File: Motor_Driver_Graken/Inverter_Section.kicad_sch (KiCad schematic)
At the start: 93 parts, among them Q1 NMOS, Q2 NMOS, Q3 NMOS, Q4 NMOS, Q5 NMOS, Q6 NMOS, U10 UCC21520DW, U6 UCC21520DW, U9 UCC21520DW

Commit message: Schematic Changes
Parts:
- removed C100: C_Small, symbol Device:C_Small
- removed R44: R_Small, symbol Device:R_Small
- added C120: 4.7u, symbol Device:C_Small
- added D11: D, symbol Device:D
- added R115: 2.2R, symbol Device:R_Small
- added R116: 10K, symbol Device:R_Small
- C42, C48, C50, C64, C66, C71, C73, C75, C76, C77, C78, C80, C89, C91: value C_Small -> 4.7u
- C43, C44, C51, C56, C65, C67, C72, C74, C79, C81, C90, C92, C97, C98, C99: value C_Small -> 0.1u
- C49, C70, C96: value C_Small -> 100n
- C52, C53, C54, C55, C68, C69, C93, C94, C95: value C_Small -> 270p
- R18, R42: value R_Small -> 10K
- R20, R21, R22, R28, R29, R30, R35, R37, R38: value R_Small -> 60.4R
- R23, R24, R26, R31, R32, R33, R39, R40, R41: value R_Small -> 2.2K
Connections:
- net 15V_ISOa: now also R115.2; no longer U6.16 (VDDA)
- net 15V_ISOb: now also C71.1, C120.1; no longer C55.1, C73.1
- net 15V_ISOc: now also C75.1, C79.1, C99.1; no longer C76.1, C97.1, C98.1
- net DIS: now also C69.1, R38.1, R38.2, R41.2; no longer C70.1, R39.1, R39.2, R42.2
- net GND2: now also C71.2, C73.1, C76.1, C97.1, C98.1, C120.2; no longer C55.2, C75.1, C79.1, C99.1
- net GNDD: now also C55.2, R39.1, R42.2, R116.2; no longer C71.2, R35.2, R42.1
- net PWM_W_HIGH: now also R35.1; no longer R37.1
- net PWM_W_LOW: now also R37.1; no longer R38.1
- net at C96.1, U10.6 (DT): now also R42.1
- removed net INA: C52.1, C68.1, C93.1, R20.2, R23.2, R28.2, R31.2, R37.2, R40.2, U10.1 (INA), U6.1 (INA), U9.1 (INA)
- removed net INB: C53.1, C69.1, C94.1, R21.2, R24.2, R29.2, R32.2, R38.2, R41.2, U10.2 (INB), U6.2 (INB), U9.2 (INB)
- new net: C70.1, R116.1, U9.6 (DT)
- new net: D11.1 (K), U6.16 (VDDA)
- new net: D11.2 (A), R115.1
- new net INuH: C52.1, R20.2, R23.2, U6.1 (INA)
- new net INuL: C53.1, R21.2, R24.2, U6.2 (INB)
- new net INvH: C55.1, R28.2, R31.2, U9.1 (INA)
- new net INvL: C68.1, R29.2, R32.2, U9.2 (INB)
- new net INwH: C93.1, R35.2, R39.2, U10.1 (INA)
- new net INwL: C94.1, R37.2, R40.2, U10.2 (INB)
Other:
- moved on the sheet: C48, C49, C52, C91, C92, Q5, Q6, R18, R20, R21, R22, R23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

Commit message: Flim Capacitors
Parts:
- removed C61, C62, C63: C_Small, symbol Device:C_Small
- removed R39, R40, R41: 2.2K, symbol Device:R_Small
- removed R47, R48, R49: R_Small, symbol Device:R_Small
- added C100, C121: 470u, symbol Device:C_Polarized
- added C157, C158, C159: 470u, symbol Device:C_Small
- added R117, R118, R44: 2.2K, symbol Device:R_Small
- C34, C59, C60: value C_Polarized -> 470u
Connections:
- net 120Vdc: now also C100.1, C121.1, C157.1, C158.1, C159.1
- net DIS: now also C52.1, C55.1, C93.1, R24.2, R31.2, R44.2; no longer C54.1, C69.1, C95.1, R26.2, R33.2
- net GND1: now also C100.2, C121.2, C157.2, C158.2, C159.2
- net GNDD: now also R117.1, R118.1, R44.1
- net INuH: now also C54.1; no longer C52.1
- net INuL: now also R26.2; no longer R24.2
- net INvH: now also C69.1, R33.2; no longer C55.1, R31.2
- net INwH: now also C95.1, R118.2; no longer C93.1
- net INwL: now also R117.2
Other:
- note added: "Aux power Supply +15v for High side and -4V for low side"
- note added: "Fc=10.98Mhz"
- note added: "Signal Filtering : Low Pass Filter"
- note added: "pulldowns to introduce current in signal lines for noise immunity"
- note removed: "Snubber Capacitors"
- moved on the sheet: C34, C53, C54, R23

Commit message: UCC21520 charctersitics
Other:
- note added: "Mosfet Characteristics"
- note added: "Switching Characteristics"
- note added: "UCC21520"
- note added: "VccI = 3 - 18V VDDA,VDDB - 6.5 to 25V(5V UVLO Version) 9.2 to 25V(8V UVLO Version) Icc - 2.0mA Ivdda,Ivddb - 2.5mA peak output source current -4A peak output sink current -6A deadtime - 20K - 200ns Is safe output supply current 36mA to 75mA VinA,VinB,Vdis - 1.8V-2V"
- moved on the sheet: C157, C158, C159

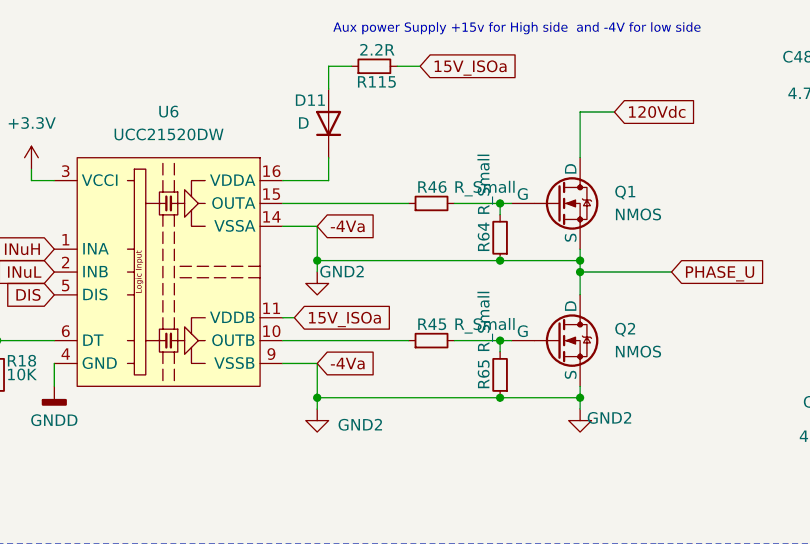
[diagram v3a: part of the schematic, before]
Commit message: adding Simulation Files
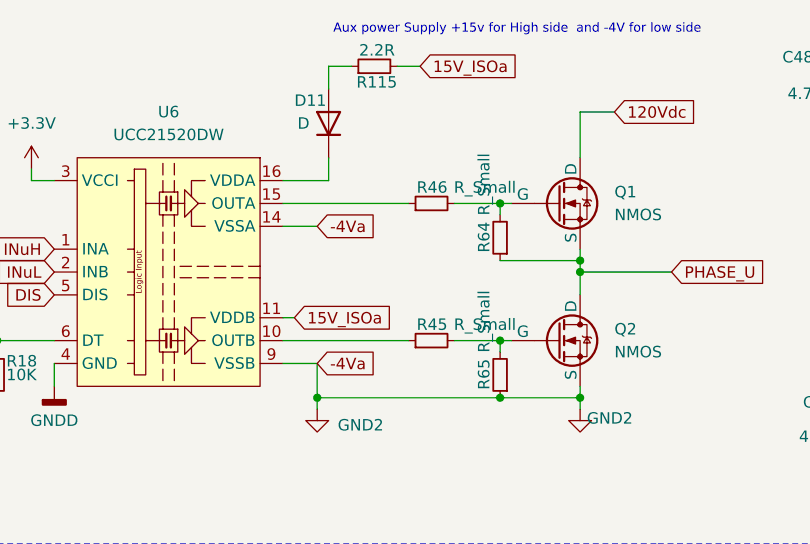
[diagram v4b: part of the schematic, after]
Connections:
- net GND2: no longer Q1.3 (S), Q2.1 (D), R64.1
- new net PHASE_U: Q1.3 (S), Q2.1 (D), R64.1
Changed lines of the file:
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@@
 (kicad_sch
-	(version 20240819)
+	(version 20241004)
 	(generator "eeschema")
 	(generator_version "8.99")
@@
 	)
 	(junction
-		(at 138.43 39.37)
-		(diameter 0)
-		(color 0 0 0 0)
-	)
-	(junction
-		(at 118.11 39.37)
-		(diameter 0)
-		(color 0 0 0 0)
-	)
-	(junction
 		(at 260.35 15.24)
 		(diameter 0)
@@
 	(wire
 		(pts
-			(xy 118.11 35.56) (xy 118.11 39.37)
-		)
-		(stroke
-			(width 0)
-			(type default)
-		)
-	)
-	(wire
-		(pts
 			(xy 40.64 55.88) (xy 46.99 55.88)
 		)
@@
 	(wire
 		(pts
-			(xy 118.11 39.37) (xy 138.43 39.37)
-		)
-		(stroke
-			(width 0)
-			(type default)
-		)
-	)
-	(wire
-		(pts
 			(xy 33.02 40.64) (xy 46.99 40.64)
 		)
@@
 	(wire
 		(pts
-			(xy 118.11 39.37) (xy 118.11 40.64)
-		)
-		(stroke
-			(width 0)
-			(type default)
-		)
-	)
-	(wire
-		(pts
 			(xy 86.36 173.99) (xy 86.36 175.26)
 		)
@@
 					(unit 1)
 				)
-			)
-		)
-	)
-	(symbol
-		(lib_id "power:GND2")
-		(at 118.11 40.64 0)
-		(mirror y)
-		(unit 1)
-		(exclude_from_sim no)
-		(in_bom yes)
-		(on_board yes)
-		(dnp no)
-		(property "Reference" "#PWR072"
-			(at 118.11 46.99 0)
-			(effects
-				(font
-					(size 1.27 1.27)
-				)
-				(hide yes)
-			)
-		)
-		(property "Value" "GND2"
-			(at 120.904 40.64 0)
-			(effects
-				(font
-					(size 1.27 1.27)
-				)
-			)
-		)
-		(property "Footprint" ""
-			(at 118.11 40.64 0)
-			(effects
-				(font
-					(size 1.27 1.27)
-				)
-				(hide yes)
-			)
-		)
-		(property "Datasheet" ""
-			(at 118.11 40.64 0)
-			(effects
-				(font
-					(size 1.27 1.27)
-				)
-				(hide yes)
-			)
-		)
-		(property "Description" "Power symbol creates a global label with name \"GND2\" , ground"
-			(at 118.11 40.64 0)
-			(effects
-				(font
-					(size 1.27 1.27)
-				)
-				(hide yes)
-			)
-		)
-		(pin "1"
-		)
-		(instances
-			(project "BESC_OWN_VERSION"
-				(path "/7c9d4969-3cbd-46ca-8216-6f71fd9792b9/d4a314ca-234a-4116-8831-95751aed0b3f"
-					(reference "#PWR072")
-					(unit 1)
-				)
